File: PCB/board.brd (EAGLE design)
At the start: 160 x 100 mm, 28 parts, among them IC1 MEGA1284P-SQUARE, IC2 MC33269D-3.3, J1 DCJ0202, Q1 CRYSTAL_16MHZ_SMD, Q2 BUZ10, U1 OPA564AIDWD

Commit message: Added MOSFET for peltier control
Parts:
- removed SV2, SV3, SV4: (no value), con-lstb:MA08-1
- removed SV5: (no value), con-lstb:MA05-1
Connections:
- removed net G_3V: Q2.1
- removed net N$34: IC1.43, SV5.4
- removed net N$7: IC1.16, SV2.8
- new net +HEATER: Q2.3
- new net HEATER_PWM: IC1.43, Q2.1
- new net PELTIER_PWM: IC1.16
- net GND: no longer Q2.3
- net N$10: no longer SV2.5
- net N$11: no longer SV2.4
- net N$12: no longer SV2.3
- net N$13: no longer SV2.2
- net N$14: no longer SV2.1
- net N$15: no longer SV3.8
- net N$16: no longer SV3.7
- net N$17: no longer SV3.6
- net N$18: no longer SV3.5
- net N$19: no longer SV3.4
- net N$20: no longer SV3.3
- net N$23: no longer SV4.1
- net N$24: no longer SV4.2
- net N$25: no longer SV4.3
- net N$26: no longer SV4.4
- net N$27: no longer SV4.5
- net N$28: no longer SV4.6
- net N$29: no longer SV4.7
- net N$30: no longer SV4.8
- net N$31: no longer SV5.1
- net N$32: no longer SV5.2
- net N$33: no longer SV5.3
- net N$35: no longer SV5.5
- net N$8: no longer SV2.7
- net N$9: no longer SV2.6
- net SCL: no longer SV3.1
- net SDA: no longer SV3.2

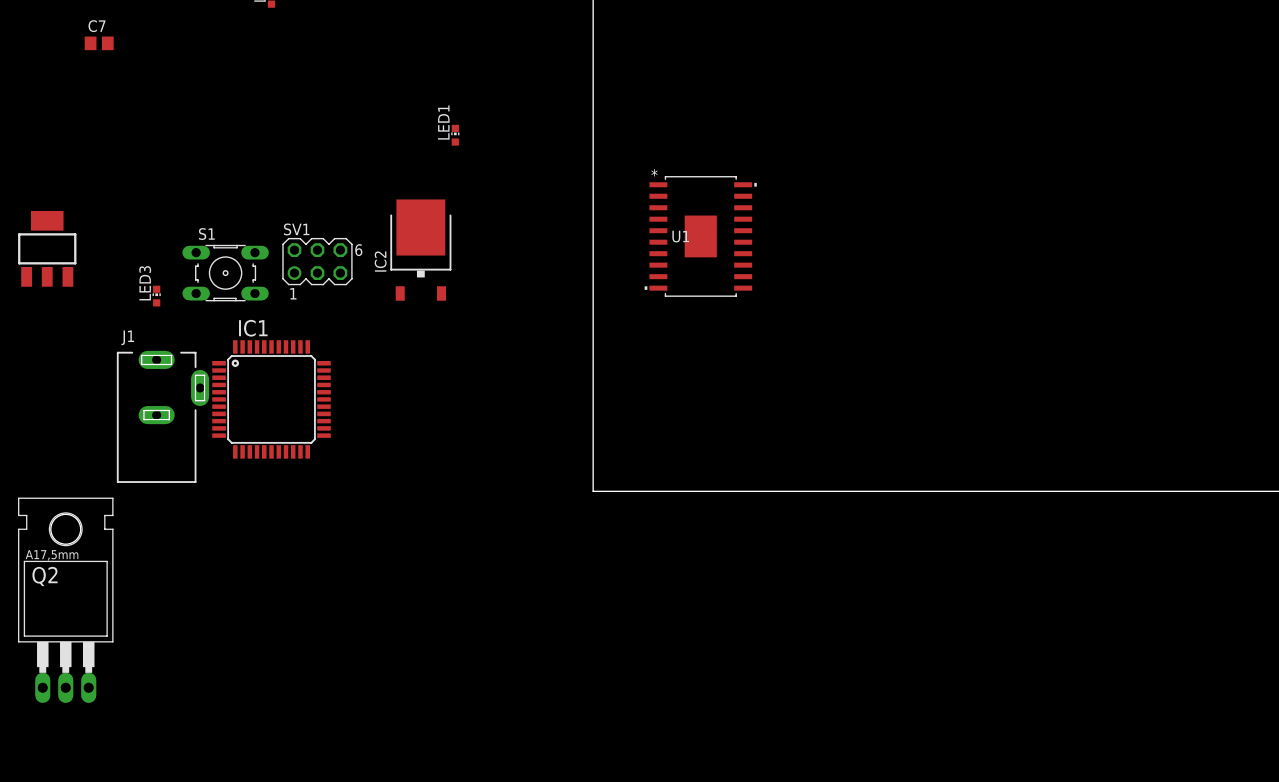
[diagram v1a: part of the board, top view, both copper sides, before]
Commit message: Finished connections for op-amp
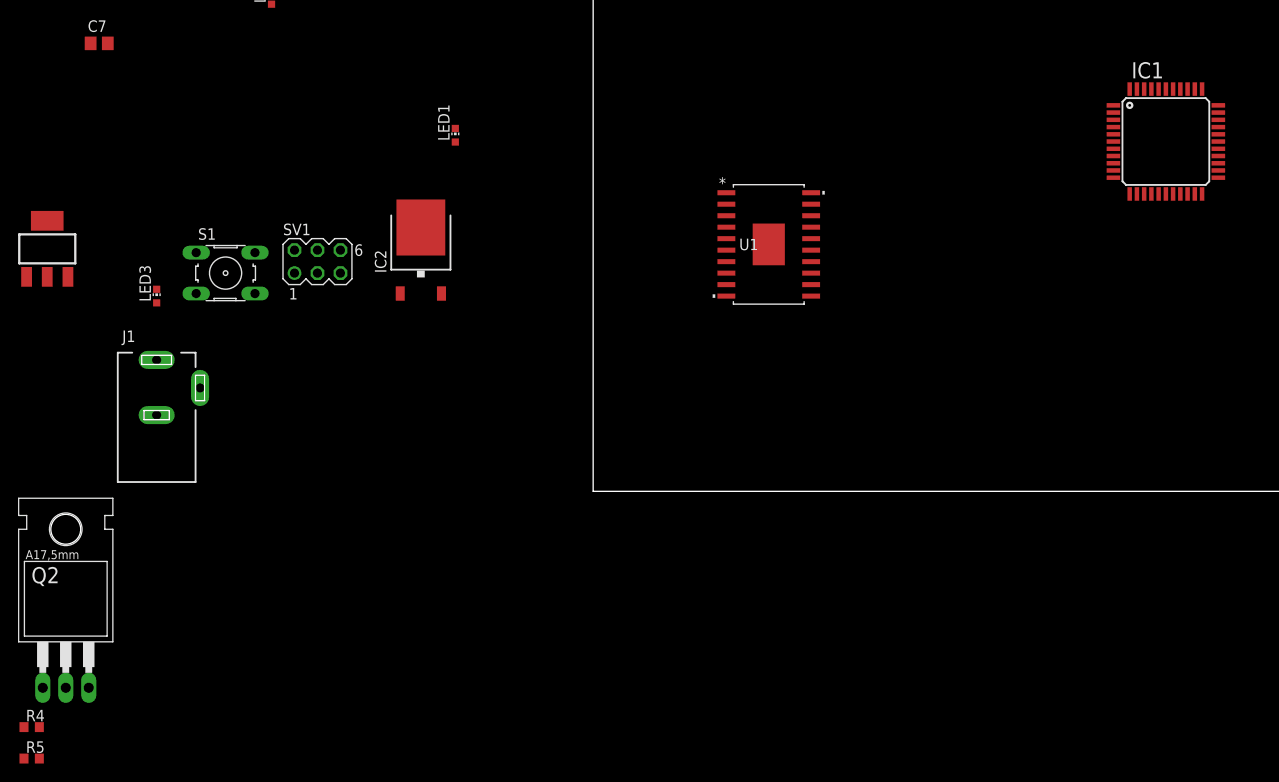
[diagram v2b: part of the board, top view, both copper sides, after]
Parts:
- added R4: 10k, rcl:R0603
- added R5: 1k, rcl:R0603
- U1: device myLibrary:DWD20_4P62X3P56 -> op-amp-library:DWD20_4P62X3P56
- moved IC1 102.9 mm to (63.3, 38.7)
- moved U1 7.57 mm to (19.4, 27.3)
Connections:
- removed net N$23: IC1.37
- removed net N$24: IC1.36
- removed net V+PWR: U1.4
- removed net V+PWR_2: U1.2
- removed net V+PWR_3: U1.3
- removed net V-PWR: U1.8
- removed net V-PWR_2: U1.7
- removed net V-_2: U1.1
- removed net V-_3: U1.10
- removed net V-_4: U1.11
- new net IFLAG: IC1.36, U1.13
- new net N$21: R4.1, R5.2
- new net N$7: R4.2, U1.12
- new net PELTIER_5V: U1.15, U1.5, U1.6
- new net TFLAG: IC1.37, U1.18
- net +12V: now also U1.2, U1.3, U1.4
- net +5V: now also U1.14, U1.17
- net GND: now also U1.1, U1.10, U1.11, U1.7, U1.8, U1.9
- net PELTIER_PWM: now also U1.16
- net V-: now also R5.1

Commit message: Fixed mosfet
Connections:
- removed net +HEATER: Q2.3
- new net -HEATER: Q2.2
- net +12V: no longer Q2.2
- net GND: now also Q2.3
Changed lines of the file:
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@@
 <contactref element="U1" pad="10"/>
 <contactref element="U1" pad="9"/>
+<contactref element="Q2" pad="3"/>
 <wire x1="57.52" y1="38.675" x2="69.12" y2="38.675" width="0" layer="19" extent="1-1"/>
 <wire x1="24.1013" y1="21.585" x2="57.52" y2="38.675" width="0" layer="19" extent="1-1"/>
@@
 <wire x1="-60.355" y1="23.71" x2="-48.26" y2="22.34" width="0" layer="19" extent="1-1"/>
 <wire x1="-60.355" y1="29.9076" x2="-60.355" y2="23.71" width="0" layer="19" extent="1-1"/>
+<wire x1="-55.77" y1="-21.72" x2="-48.26" y2="8.43" width="0" layer="19" extent="1-1"/>
 </signal>
 <signal name="+5V">
@@
 </signal>
 <signal name="+12V">
-<contactref element="Q2" pad="2"/>
 <contactref element="U1" pad="2"/>
 <contactref element="U1" pad="3"/>
 <contactref element="U1" pad="4"/>
-<wire x1="14.7287" y1="29.205" x2="-58.31" y2="-21.72" width="0" layer="19" extent="1-1"/>
-<wire x1="14.7287" y1="30.475" x2="14.7287" y2="29.205" width="0" layer="19" extent="1-1"/>
-<wire x1="14.7287" y1="31.745" x2="14.7287" y2="30.475" width="0" layer="19" extent="1-1"/>
-</signal>
-<signal name="+HEATER">
-<contactref element="Q2" pad="3"/>
-</signal>
-<signal name="-HEATER">
+<wire x1="14.7287" y1="30.475" x2="14.7287" y2="31.745" width="0" layer="19" extent="1-1"/>
+<wire x1="14.7287" y1="29.205" x2="14.7287" y2="30.475" width="0" layer="19" extent="1-1"/>
 </signal>
 <signal name="N$7">
@@
 <wire x1="24.1013" y1="30.475" x2="64.92" y2="44.475" width="0" layer="19" extent="1-1"/>
 </signal>
+<signal name="-HEATER">
+<contactref element="Q2" pad="2"/>
+</signal>
+<signal name="+HEATER">
+</signal>
 </signals>

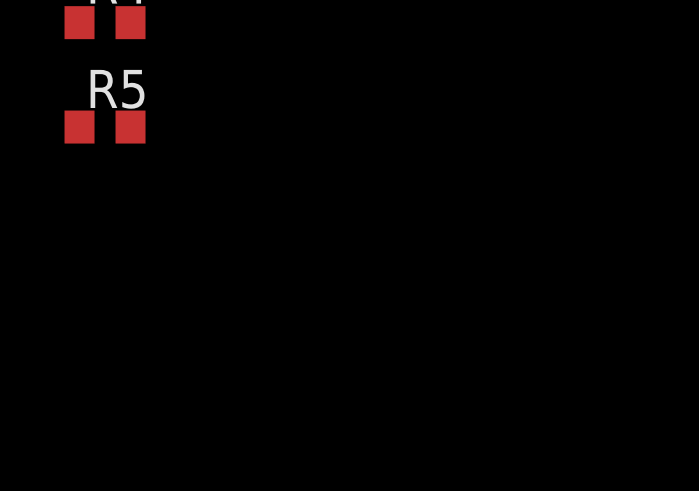
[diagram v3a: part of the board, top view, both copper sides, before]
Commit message: Added connector for heater
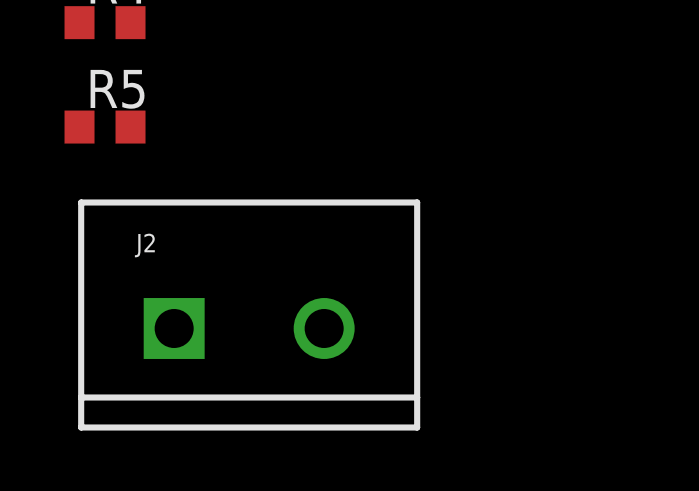
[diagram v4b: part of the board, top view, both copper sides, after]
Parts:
- added J2: (no value), SparkFun-Connectors:SCREWTERMINAL-5MM-2
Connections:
- removed net N$1: C1.1, J1.1, LDO1.P$1
- removed net V+: U1.19
- removed net V-: R5.1, U1.20
- new net +HEATER: J2.1
- net +12V: now also C1.1, J1.1, LDO1.P$1, U1.19
- net -HEATER: now also J2.2
- net GND: now also R5.1, U1.20
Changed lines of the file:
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@@
 <layer number="56" name="wert" color="7" fill="1" visible="no" active="no"/>
 <layer number="57" name="tCAD" color="7" fill="1" visible="no" active="no"/>
+<layer number="59" name="tCarbon" color="7" fill="1" visible="no" active="no"/>
+<layer number="60" name="bCarbon" color="7" fill="1" visible="no" active="no"/>
 <layer number="88" name="SimResults" color="9" fill="1" visible="no" active="no"/>
 <layer number="89" name="SimProbes" color="9" fill="1" visible="no" active="no"/>
@@
 <layer number="97" name="Info" color="7" fill="1" visible="no" active="no"/>
 <layer number="98" name="Guide" color="6" fill="1" visible="no" active="no"/>
+<layer number="99" name="SpiceOrder" color="7" fill="1" visible="no" active="no"/>
 <layer number="100" name="Muster" color="7" fill="1" visible="no" active="no"/>
 <layer number="101" name="Patch_Top" color="12" fill="4" visible="yes" active="yes"/>
@@
 <layer number="111" name="LPC17xx" color="7" fill="1" visible="yes" active="yes"/>
 <layer number="112" name="tSilk" color="7" fill="1" visible="yes" active="yes"/>
+<layer number="113" name="IDFDebug" color="4" fill="1" visible="no" active="no"/>
+<layer number="114" name="Badge_Outline" color="7" fill="1" visible="no" active="no"/>
+<layer number="115" name="ReferenceISLANDS" color="7" fill="1" visible="no" active="no"/>
 <layer number="116" name="Patch_BOT" color="9" fill="4" visible="yes" active="yes"/>
+<layer number="117" name="PM_Ref" color="7" fill="1" visible="no" active="no"/>
+<layer number="118" name="Rect_Pads" color="7" fill="1" visible="no" active="no"/>
+<layer number="119" name="PF_Ref" color="7" fill="1" visible="no" active="no"/>
+<layer number="120" name="WFL_Ref" color="7" fill="1" visible="no" active="no"/>
 <layer number="121" name="_tsilk" color="7" fill="1" visible="yes" active="yes"/>
 <layer number="122" name="_bsilk" color="7" fill="1" visible="yes" active="yes"/>
@@
 <layer number="127" name="_tValues" color="7" fill="1" visible="yes" active="yes"/>
 <layer number="128" name="_bValues" color="7" fill="1" visible="yes" active="yes"/>
+<layer number="129" name="Mask" color="7" fill="1" visible="no" active="no"/>
 <layer number="131" name="tAdjust" color="7" fill="1" visible="yes" active="yes"/>
 <layer number="132" name="bAdjust" color="7" fill="1" visible="yes" active="yes"/>
@@
 <layer number="223" name="223bmp" color="24" fill="1" visible="no" active="no"/>
 <layer number="224" name="224bmp" color="25" fill="1" visible="no" active="no"/>
+<layer number="225" name="225bmp" color="7" fill="1" visible="no" active="no"/>
+<layer number="226" name="226bmp" color="7" fill="1" visible="no" active="no"/>
+<layer number="227" name="227bmp" color="7" fill="1" visible="no" active="no"/>
+<layer number="228" name="228bmp" color="7" fill="1" visible="no" active="no"/>
+<layer number="229" name="229bmp" color="7" fill="1" visible="no" active="no"/>
+<layer number="230" name="230bmp" color="7" fill="1" visible="no" active="no"/>
+<layer number="231" name="231bmp" color="7" fill="1" visible="no" active="no"/>
+<layer number="232" name="Eagle3D_PG2" color="7" fill="1" visible="no" active="no"/>
+<layer number="233" name="Eagle3D_PG3" color="7" fill="1" visible="no" active="no"/>
 <layer number="248" name="Housing" color="7" fill="1" visible="yes" active="yes"/>
 <layer number="249" name="Edge" color="7" fill="1" visible="yes" active="yes"/>
@@
 <layer number="251" name="SMDround" color="12" fill="11" visible="no" active="no"/>
 <layer number="254" name="cooling" color="7" fill="1" visible="yes" active="yes"/>
+<layer number="255" name="routoute" color="7" fill="1" visible="no" active="no"/>
 </layers>
 <board>
@@
 <attribute name="VENDOR" value="Texas Instruments" x="19.415" y="27.3" size="1.778" layer="27" display="off"/>
 </element>
+<element name="J2" library="SparkFun-Connectors" package="SCREWTERMINAL-5MM-2" value="" x="-59.775" y="-36.26" smashed="yes">
+<attribute name="NAME" x="-61.045" y="-33.72" size="0.6096" layer="25" font="vector" ratio="20"/>
+<attribute name="SF_SKU" value="PRT-08432" x="-59.775" y="-36.26" size="1.778" layer="27" display="off"/>
+<attribute name="VALUE" x="-61.045" y="-34.99" size="0.6096" layer="27" font="vector" ratio="20"/>
+</element>
 </elements>
 <signals>
-<signal name="N$1">
-<contactref element="C1" pad="1"/>
-<contactref element="LDO1" pad="P$1"/>
-<contactref element="J1" pad="1"/>
-<wire x1="-48.26" y1="14.53" x2="-18.73" y2="57.15" width="0" layer="19" extent="1-1"/>
-<wire x1="-62.641" y1="23.71" x2="-48.26" y2="14.53" width="0" layer="19" extent="1-1"/>
-</signal>
 <signal name="GND">
 <contactref element="LDO1" pad="P$2"/>
@@
 <contactref element="U1" pad="9"/>
 <contactref element="Q2" pad="3"/>
+<contactref element="R5" pad="1"/>
+<contactref element="U1" pad="20"/>
 <wire x1="57.52" y1="38.675" x2="69.12" y2="38.675" width="0" layer="19" extent="1-1"/>
-<wire x1="24.1013" y1="21.585" x2="57.52" y2="38.675" width="0" layer="19" extent="1-1"/>
-<wire x1="14.7287" y1="21.585" x2="24.1013" y2="21.585" width="0" layer="19" extent="1-1"/>
-<wire x1="14.7287" y1="22.855" x2="14.7287" y2="21.585" width="0" layer="19" extent="1-1"/>
-<wire x1="14.7287" y1="24.125" x2="14.7287" y2="22.855" width="0" layer="19" extent="1-1"/>
-<wire x1="14.7287" y1="25.395" x2="14.7287" y2="24.125" width="0" layer="19" extent="1-1"/>
-<wire x1="14.7287" y1="33.015" x2="14.7287" y2="25.395" width="0" layer="19" extent="1-1"/>
+<wire x1="24.1013" y1="33.015" x2="57.52" y2="38.675" width="0" layer="19" extent="1-1"/>
+<wire x1="14.7287" y1="33.015" x2="24.1013" y2="33.015" width="0" layer="19" extent="1-1"/>
+<wire x1="14.7287" y1="25.395" x2="14.7287" y2="33.015" width="0" layer="19" extent="1-1"/>
+<wire x1="14.7287" y1="24.125" x2="14.7287" y2="25.395" width="0" layer="19" extent="1-1"/>
+<wire x1="14.7287" y1="22.855" x2="14.7287" y2="24.125" width="0" layer="19" extent="1-1"/>
+<wire x1="14.7287" y1="21.585" x2="14.7287" y2="22.855" width="0" layer="19" extent="1-1"/>
+<wire x1="24.1013" y1="21.585" x2="14.7287" y2="21.585" width="0" layer="19" extent="1-1"/>
 <wire x1="-15.24" y1="40.12" x2="14.7287" y2="33.015" width="0" layer="19" extent="1-1"/>
 <wire x1="-16.83" y1="57.15" x2="-15.24" y2="40.12" width="0" layer="19" extent="1-1"/>
@@
 <wire x1="-60.355" y1="29.9076" x2="-60.355" y2="23.71" width="0" layer="19" extent="1-1"/>
 <wire x1="-55.77" y1="-21.72" x2="-48.26" y2="8.43" width="0" layer="19" extent="1-1"/>
+<wire x1="-62.93" y1="-29.545" x2="-55.77" y2="-21.72" width="0" layer="19" extent="1-1"/>
 </signal>
 <signal name="+5V">
@@
 <contactref element="U1" pad="3"/>
 <contactref element="U1" pad="4"/>
+<contactref element="C1" pad="1"/>
+<contactref element="LDO1" pad="P$1"/>
+<contactref element="J1" pad="1"/>
+<contactref element="U1" pad="19"/>
+<wire x1="14.7287" y1="31.745" x2="24.1013" y2="31.745" width="0" layer="19" extent="1-1"/>
 <wire x1="14.7287" y1="30.475" x2="14.7287" y2="31.745" width="0" layer="19" extent="1-1"/>
 <wire x1="14.7287" y1="29.205" x2="14.7287" y2="30.475" width="0" layer="19" extent="1-1"/>
+<wire x1="-18.73" y1="57.15" x2="14.7287" y2="31.745" width="0" layer="19" extent="1-1"/>
+<wire x1="-48.26" y1="14.53" x2="-18.73" y2="57.15" width="0" layer="19" extent="1-1"/>
+<wire x1="-62.641" y1="23.71" x2="-48.26" y2="14.53" width="0" layer="19" extent="1-1"/>
 </signal>
 <signal name="N$7">
@@
 <contactref element="R5" pad="2"/>
 <wire x1="-62.93" y1="-26.065" x2="-61.23" y2="-29.545" width="0" layer="19" extent="1-1"/>
-</signal>
-<signal name="V-">
-<contactref element="R5" pad="1"/>
-<contactref element="U1" pad="20"/>
-<wire x1="24.1013" y1="33.015" x2="-62.93" y2="-29.545" width="0" layer="19" extent="1-1"/>
-</signal>
-<signal name="V+">
-<contactref element="U1" pad="19"/>
 </signal>
 <signal name="PELTIER_5V">
@@
 <signal name="-HEATER">
 <contactref element="Q2" pad="2"/>
+<contactref element="J2" pad="2"/>
+<wire x1="-58.31" y1="-21.72" x2="-54.775" y2="-36.26" width="0" layer="19" extent="1-1"/>
 </signal>
 <signal name="+HEATER">
+<contactref element="J2" pad="1"/>
 </signal>
 </signals>

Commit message: Placing on board
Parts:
- removed J2: (no value), SparkFun-Connectors:SCREWTERMINAL-5MM-2
- added HEATER_CONNECTOR, PELTIER_CONNECTOR: (no value), SparkFun-Connectors:SCREWTERMINAL-5MM-2
- added SV2, SV4: (no value), con-lstb:MA08-1
- added SV3: (no value), con-lstb:MA04-1
- added SV5: (no value), con-lstb:MA07-1
- moved R4 119.2 mm to (45.3, 25.7)
- moved R5 119.2 mm to (45.3, 22.2)
- moved Q2 110.8 mm to (50.5, 5.62), turned to 270 degrees
- moved C5 89.3 mm to (31.0, 41.5), turned to 270 degrees
- moved SV1 78.3 mm to (43.4, 51.2)
- moved Q1 76.6 mm to (29.7, 35.0)
- moved LED2 71.3 mm to (35.7, 57.3), turned to 90 degrees
- moved R3 70.8 mm to (42.6, 57.4)
- moved LDO1 70.5 mm to (9.54, 33.3)
- moved C7 64.3 mm to (9.57, 46.4), turned to 270 degrees
- moved C4 62.1 mm to (5.75, 30.2)
- moved C3 57.2 mm to (14.0, 58.0)
- moved J1 54.1 mm to (5.87, 11.3)
- moved LED3 52.5 mm to (2.15, 36.3), turned to 180 degrees
- moved C6 49.8 mm to (25.2, 38.3)
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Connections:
- net N$7 renamed ISET
- net +HEATER: now also HEATER_CONNECTOR.1; no longer J2.1
- net -HEATER: now also HEATER_CONNECTOR.2; no longer J2.2
- net GND: now also PELTIER_CONNECTOR.2
- net IFLAG: now also SV2.2
- net N$10: now also SV5.5
- net N$11: now also SV5.4
- net N$12: now also SV5.3
- net N$13: now also SV5.2
- net N$14: now also SV5.1
- net N$15: now also SV4.8
- net N$16: now also SV4.7
- net N$17: now also SV4.6
- net N$18: now also SV4.5
- net N$19: now also SV4.4
- net N$20: now also SV4.3
- net N$25: now also SV2.3
- net N$26: now also SV2.4
- net N$27: now also SV2.5
- net N$28: now also SV2.6
- net N$29: now also SV2.7
- net N$30: now also SV2.8
- net N$31: now also SV3.1
- net N$32: now also SV3.2
- net N$33: now also SV3.3
- net N$35: now also SV3.4
- net N$8: now also SV5.7
- net N$9: now also SV5.6
- net PELTIER_5V: now also PELTIER_CONNECTOR.1
- net SCL: now also SV4.1
- net SDA: now also SV4.2
- net TFLAG: now also SV2.1
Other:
- board size 160 x 100 mm -> 100 x 60 mm

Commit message: started routing
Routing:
- net RESET: track 0.00 -> 97.3 mm, vias 0 -> 4
- net N$2: track 0.00 -> 64.5 mm, vias 0 -> 2
- net IFLAG: track 0.00 -> 46.1 mm, vias 0 -> 4
- net PELTIER_5V: track 0.00 -> 39.6 mm
- net +5V: track 0.00 -> 37.4 mm, vias 0 -> 2
- net PELTIER_PWM: track 0.00 -> 35.0 mm, vias 0 -> 2
- net HEATER_PWM: track 0.00 -> 33.9 mm, vias 0 -> 2
- net N$4: track 0.00 -> 31.0 mm, vias 0 -> 2
- net +12V: track 0.00 -> 30.5 mm
- net SCK: track 0.00 -> 27.3 mm
- net N$3: track 0.00 -> 27.1 mm, vias 0 -> 2
- net TFLAG: track 0.00 -> 26.3 mm
- net N$31: track 0.00 -> 20.9 mm
- net +3V3: track 0.00 -> 20.7 mm, vias 0 -> 2
- net N$32: track 0.00 -> 20.0 mm
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- added copper zone on layer 1, net +5V
- added copper zone on layer 1, net GND
- added copper zone on layer 16, net GND
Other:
- board size 100 x 60 mm -> 79 x 60 mm

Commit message: finished routing PCB
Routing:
- net +5V: track 37.4 -> 110.3 mm, vias 2 -> 9
- net TFLAG: track 26.3 -> 64.1 mm, vias 0 -> 2
- net ISET: track 0.00 -> 26.4 mm, vias 0 -> 2
- net N$8: track 0.00 -> 23.0 mm
- net IFLAG: track 46.1 -> 69.1 mm
- net SCL: track 0.00 -> 21.2 mm
- net N$9: track 0.00 -> 21.1 mm
- net N$25: track 0.00 -> 21.1 mm
- net N$10: track 0.00 -> 19.5 mm, vias 0 -> 3
- net SDA: track 0.00 -> 19.3 mm
- net MISO: track 0.00 -> 19.3 mm
- net N$26: track 0.00 -> 18.9 mm
- net N$20: track 0.00 -> 17.5 mm
- net MOSI: track 0.00 -> 17.0 mm, vias 0 -> 2
- net N$27: track 0.00 -> 16.8 mm
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
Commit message: finished routing PCB with added pins; need silkscreen!
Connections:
- net +5V: now also IC1.17, IC1.38
- net GND: now also IC1.18, IC1.39
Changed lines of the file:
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@@
 <wire x1="17.78" y1="57.785" x2="15.06" y2="57.785" width="0.2" layer="1"/>
 <wire x1="15.06" y1="57.785" x2="14.83" y2="58.015" width="0.2" layer="1"/>
+<contactref element="IC1" pad="18"/>
+<contactref element="IC1" pad="39"/>
 </signal>
 <signal name="+5V">
@@
 <wire x1="41.275" y1="46.99" x2="41.68685" y2="46.99" width="0.1524" layer="16"/>
 <wire x1="41.68685" y1="46.99" x2="43.56365" y2="48.8668" width="0.1524" layer="16"/>
+<contactref element="IC1" pad="17"/>
+<contactref element="IC1" pad="38"/>
+<wire x1="54.61" y1="33.02" x2="57.58" y2="38.2" width="0" layer="19" extent="1-1"/>
+<wire x1="56.78" y1="26.6" x2="54.61" y2="33.02" width="0" layer="19" extent="1-1"/>
 </signal>
 <signal name="N$5">
